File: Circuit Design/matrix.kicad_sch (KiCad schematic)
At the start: 198 parts

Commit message: all the routing is done
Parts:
- gave numbers to parts that had none: 198

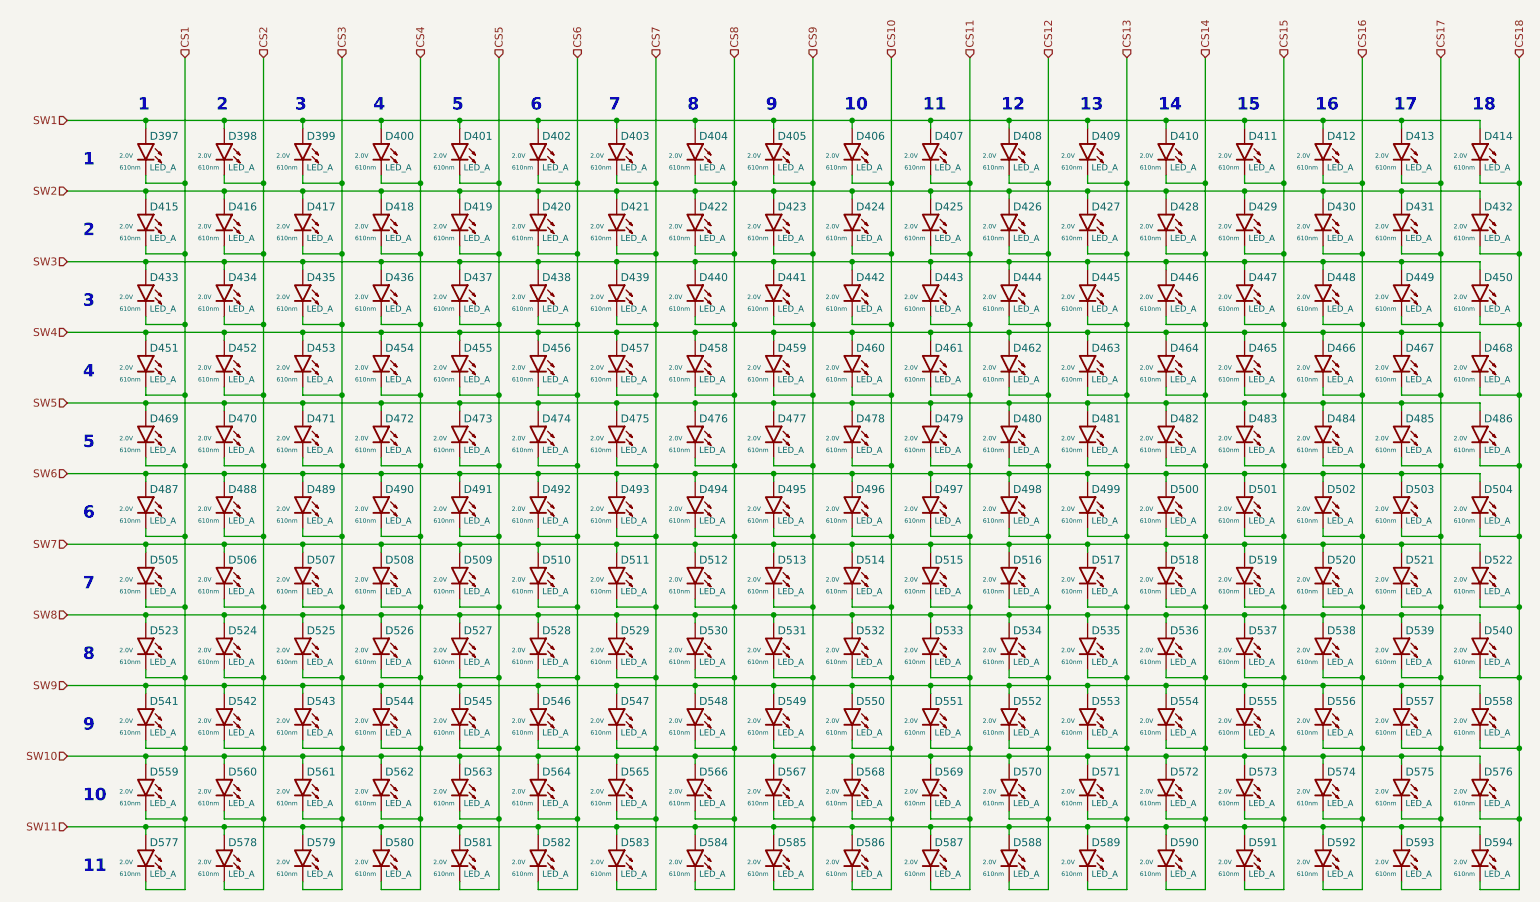
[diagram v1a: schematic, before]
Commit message: added IS31FL3731 and, edited its page
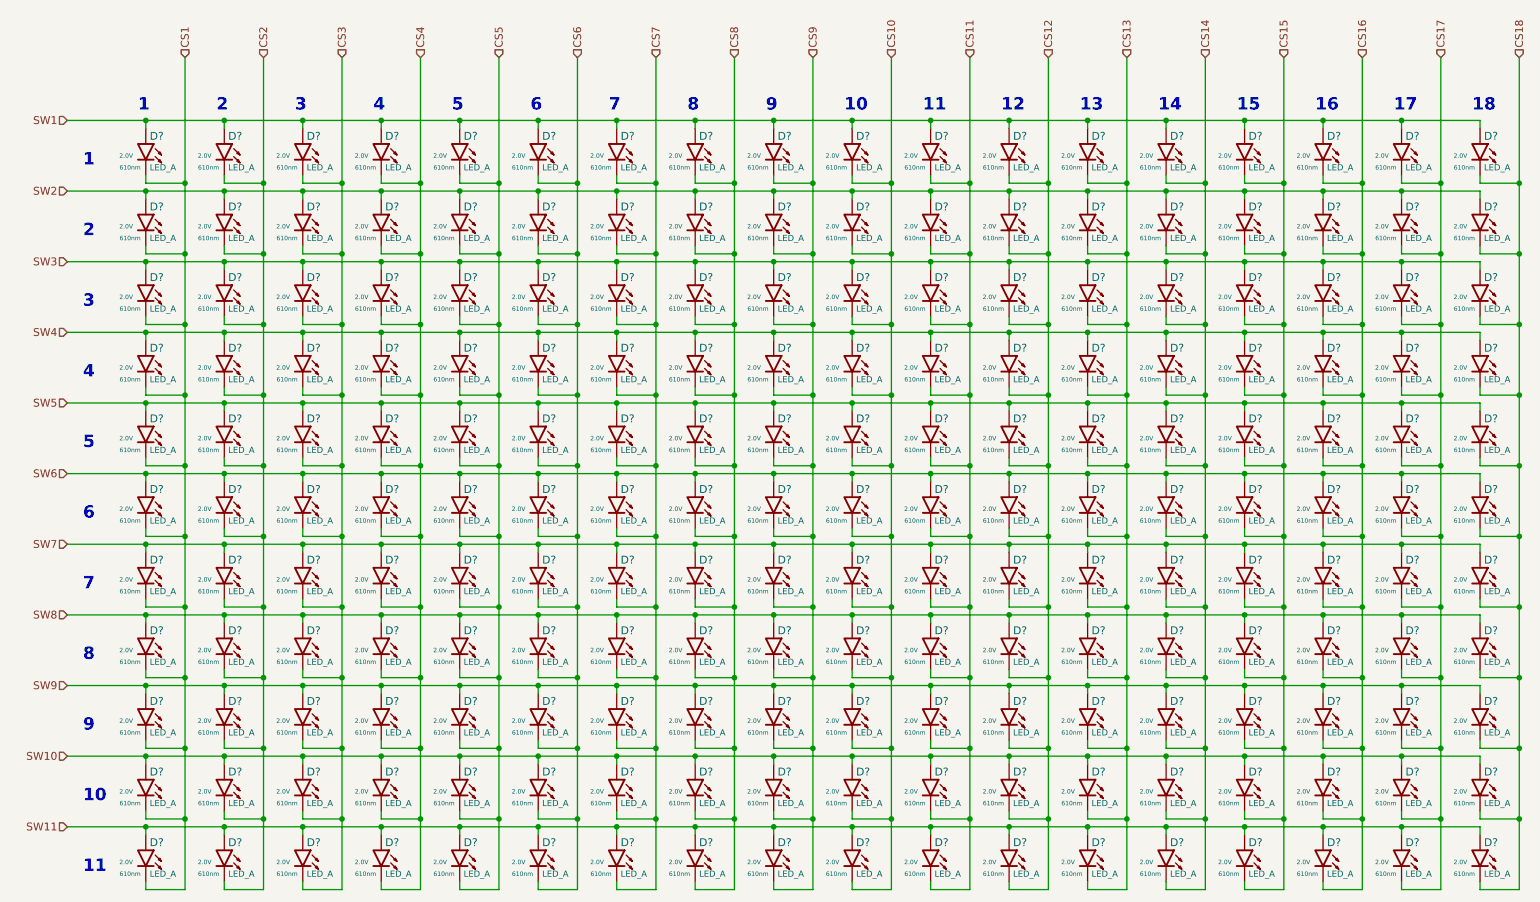
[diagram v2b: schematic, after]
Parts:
- renumbered D539 to D?, D530 to D?, D552 to D?, D586 to D?, D589 to D?, D459 to D?, D480 to D?, D506 to D?, D400 to D?, D527 to D?, D505 to D?, D487 to D?, D416 to D?, D572 to D?, D451 to D?, D435 to D?, D588 to D?, D469 to D?, D424 to D?, D534 to D?, D402 to D?, D520 to D?, D476 to D?, D526 to D?, D445 to D?, D502 to D?, D432 to D?, D462 to D?, D559 to D?, D446 to D?, D518 to D?, D512 to D?, D556 to D?, D563 to D?, D494 to D?, D524 to D?, D574 to D?, D428 to D?, D415 to D?, D580 to D?, D496 to D?, D399 to D?, D533 to D?, D444 to D?, D554 to D?, D472 to D?, D452 to D?, D427 to D?, D422 to D?, D564 to D?, D509 to D?, D522 to D?, D513 to D?, D417 to D?, D570 to D?, D503 to D?, D434 to D?, D409 to D?, D541 to D?, D557 to D?, D575 to D?, D508 to D?, D540 to D?, D404 to D?, D438 to D?, D493 to D?, D516 to D?, D519 to D?, D547 to D?, D555 to D?, D560 to D?, D529 to D?, D571 to D?, D486 to D?, D573 to D?, D455 to D?, D441 to D?, D591 to D?, D450 to D?, D420 to D?, D507 to D?, D490 to D?, D577 to D?, D514 to D?, D474 to D?, D465 to D?, D473 to D?, D544 to D?, D398 to D?, D443 to D?, D498 to D?, D517 to D?, D475 to D?, D423 to D?, D463 to D?, D483 to D?, D548 to D?, D397 to D?, D553 to D?, D403 to D?, D419 to D?, D590 to D?, D406 to D?, D414 to D?, D471 to D?, D479 to D?, D448 to D?, D511 to D?, D567 to D?, D426 to D?, D458 to D?, D562 to D?, D583 to D?, D464 to D?, D543 to D?, D457 to D?, D515 to D?, D531 to D?, D523 to D?, D500 to D?, D430 to D?, D453 to D?, D470 to D?, D576 to D?, D442 to D?, D407 to D?, D456 to D?, D538 to D?, D592 to D?, D551 to D?, D581 to D?, D521 to D?, D495 to D?, D549 to D?, D578 to D?, D466 to D?, D405 to D?, D594 to D?, D532 to D?, D566 to D?, D436 to D?, D558 to D?, D546 to D?, D439 to D?, D449 to D?, D525 to D?, D565 to D?, D413 to D?, D593 to D?, D569 to D?, D408 to D?, D440 to D?, D429 to D?, D510 to D?, D460 to D?, D501 to D?, D489 to D?, D431 to D?, D482 to D?, D550 to D?, D584 to D?, D537 to D?, D433 to D?, D484 to D?, D579 to D?, D536 to D?, D454 to D?, D545 to D?, D561 to D?, D478 to D?, D447 to D?, D461 to D?, D542 to D?, D410 to D?, D477 to D?, D491 to D?, D437 to D?, D528 to D?, D492 to D?, D421 to D?, D411 to D?, D485 to D?, D585 to D?, D488 to D?, D481 to D?, D412 to D?, D467 to D?, D425 to D?, D582 to D?, D499 to D?, D468 to D?, D535 to D?, D418 to D?, D568 to D?, D504 to D?, D497 to D?, D401 to D?, D587 to D?

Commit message: last commit before 0805 migration
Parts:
- removed D? (x198): LED_A, CoF_Diode:LED-0603, symbol CoE_Diode:LED_A
- added D1011, D1012, D1013, D1014, D1015, D1016, D1017, D1018, D1019, D1020, D1021, D1022, D1023, D1024, D1025, D1026, D1027, D1028, D1029, D1030, D1031, D1032, D1033, D1034, D1035, D1036, D1037, D1038, D1039, D1040, D1041, D1042, D1043, D1044, D1045, D1046, D1047, D1048, D1049, D1050, D1051, D1052, D1053, D1054, D1055, D1056, D1057, D1058, D1059, D1060, D1061, D1062, D1063, D1064, D1065, D1066, D1067, D1068, D1069, D1070, D1071, D1072, D1073, D1074, D1075, D1076, D1077, D1078, D1079, D1080, D1081, D1082, D1083, D1084, D1085, D1086, D1087, D1088, D1089, D1090, D1091, D1092, D1093, D1094, D1095, D1096, D1097, D1098, D1099, D1100, D1101, D1102, D1103, D1104, D1105, D1106, D1107, D1108, D1109, D1110, D1111, D1112, D1113, D1114, D1115, D1116, D1117, D1118, D1119, D1120, D1121, D1122, D1123, D1124, D1125, D1126, D1127, D1128, D1129, D1130, D1131, D1132, D1133, D1134, D1135, D1136, D1137, D1138, D1139, D1140, D1141, D1142, D1143, D1144, D1145, D1146, D1147, D1148, D1149, D1150, D1151, D1152, D1153, D1154: LED_O, CoF_Diode:LED-0402, symbol CoE_Diode:LED_O
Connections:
- new net CA1: D1011.1 (K), D1012.1 (K), D1013.1 (K), D1014.1 (K), D1015.1 (K), D1016.1 (K), D1017.1 (K), D1018.1 (K), D1027.2 (A), D1043.2 (A), D1059.2 (A), D1075.2 (A), D1091.2 (A), D1107.2 (A), D1123.2 (A), D1139.2 (A)
- new net CA2: D1011.2 (A), D1027.1 (K), D1028.1 (K), D1029.1 (K), D1030.1 (K), D1031.1 (K), D1032.1 (K), D1033.1 (K), D1034.1 (K), D1044.2 (A), D1060.2 (A), D1076.2 (A), D1092.2 (A), D1108.2 (A), D1124.2 (A), D1140.2 (A)
- new net CA3: D1012.2 (A), D1028.2 (A), D1043.1 (K), D1044.1 (K), D1045.1 (K), D1046.1 (K), D1047.1 (K), D1048.1 (K), D1049.1 (K), D1050.1 (K), D1061.2 (A), D1077.2 (A), D1093.2 (A), D1109.2 (A), D1125.2 (A), D1141.2 (A)
- new net CA4: D1013.2 (A), D1029.2 (A), D1045.2 (A), D1059.1 (K), D1060.1 (K), D1061.1 (K), D1062.1 (K), D1063.1 (K), D1064.1 (K), D1065.1 (K), D1066.1 (K), D1078.2 (A), D1094.2 (A), D1110.2 (A), D1126.2 (A), D1142.2 (A)
- new net CA5: D1014.2 (A), D1030.2 (A), D1046.2 (A), D1062.2 (A), D1075.1 (K), D1076.1 (K), D1077.1 (K), D1078.1 (K), D1079.1 (K), D1080.1 (K), D1081.1 (K), D1082.1 (K), D1095.2 (A), D1111.2 (A), D1127.2 (A), D1143.2 (A)
- new net CA6: D1015.2 (A), D1031.2 (A), D1047.2 (A), D1063.2 (A), D1079.2 (A), D1091.1 (K), D1092.1 (K), D1093.1 (K), D1094.1 (K), D1095.1 (K), D1096.1 (K), D1097.1 (K), D1098.1 (K), D1112.2 (A), D1128.2 (A), D1144.2 (A)
- new net CA7: D1016.2 (A), D1032.2 (A), D1048.2 (A), D1064.2 (A), D1080.2 (A), D1096.2 (A), D1107.1 (K), D1108.1 (K), D1109.1 (K), D1110.1 (K), D1111.1 (K), D1112.1 (K), D1113.1 (K), D1114.1 (K), D1129.2 (A), D1145.2 (A)
- new net CA8: D1017.2 (A), D1033.2 (A), D1049.2 (A), D1065.2 (A), D1081.2 (A), D1097.2 (A), D1113.2 (A), D1123.1 (K), D1124.1 (K), D1125.1 (K), D1126.1 (K), D1127.1 (K), D1128.1 (K), D1129.1 (K), D1130.1 (K), D1146.2 (A)
- new net CA9: D1018.2 (A), D1034.2 (A), D1050.2 (A), D1066.2 (A), D1082.2 (A), D1098.2 (A), D1114.2 (A), D1130.2 (A), D1139.1 (K), D1140.1 (K), D1141.1 (K), D1142.1 (K), D1143.1 (K), D1144.1 (K), D1145.1 (K), D1146.1 (K)
- new net CB1: D1019.1 (K), D1020.1 (K), D1021.1 (K), D1022.1 (K), D1023.1 (K), D1024.1 (K), D1025.1 (K), D1026.1 (K), D1035.2 (A), D1051.2 (A), D1067.2 (A), D1083.2 (A), D1099.2 (A), D1115.2 (A), D1131.2 (A), D1147.2 (A)
- new net CB2: D1019.2 (A), D1035.1 (K), D1036.1 (K), D1037.1 (K), D1038.1 (K), D1039.1 (K), D1040.1 (K), D1041.1 (K), D1042.1 (K), D1052.2 (A), D1068.2 (A), D1084.2 (A), D1100.2 (A), D1116.2 (A), D1132.2 (A), D1148.2 (A)
- new net CB3: D1020.2 (A), D1036.2 (A), D1051.1 (K), D1052.1 (K), D1053.1 (K), D1054.1 (K), D1055.1 (K), D1056.1 (K), D1057.1 (K), D1058.1 (K), D1069.2 (A), D1085.2 (A), D1101.2 (A), D1117.2 (A), D1133.2 (A), D1149.2 (A)
- new net CB4: D1021.2 (A), D1037.2 (A), D1053.2 (A), D1067.1 (K), D1068.1 (K), D1069.1 (K), D1070.1 (K), D1071.1 (K), D1072.1 (K), D1073.1 (K), D1074.1 (K), D1086.2 (A), D1102.2 (A), D1118.2 (A), D1134.2 (A), D1150.2 (A)
- new net CB5: D1022.2 (A), D1038.2 (A), D1054.2 (A), D1070.2 (A), D1083.1 (K), D1084.1 (K), D1085.1 (K), D1086.1 (K), D1087.1 (K), D1088.1 (K), D1089.1 (K), D1090.1 (K), D1103.2 (A), D1119.2 (A), D1135.2 (A), D1151.2 (A)
- new net CB6: D1023.2 (A), D1039.2 (A), D1055.2 (A), D1071.2 (A), D1087.2 (A), D1099.1 (K), D1100.1 (K), D1101.1 (K), D1102.1 (K), D1103.1 (K), D1104.1 (K), D1105.1 (K), D1106.1 (K), D1120.2 (A), D1136.2 (A), D1152.2 (A)
- new net CB7: D1024.2 (A), D1040.2 (A), D1056.2 (A), D1072.2 (A), D1088.2 (A), D1104.2 (A), D1115.1 (K), D1116.1 (K), D1117.1 (K), D1118.1 (K), D1119.1 (K), D1120.1 (K), D1121.1 (K), D1122.1 (K), D1137.2 (A), D1153.2 (A)
- new net CB8: D1025.2 (A), D1041.2 (A), D1057.2 (A), D1073.2 (A), D1089.2 (A), D1105.2 (A), D1121.2 (A), D1131.1 (K), D1132.1 (K), D1133.1 (K), D1134.1 (K), D1135.1 (K), D1136.1 (K), D1137.1 (K), D1138.1 (K), D1154.2 (A)
- new net CB9: D1026.2 (A), D1042.2 (A), D1058.2 (A), D1074.2 (A), D1090.2 (A), D1106.2 (A), D1122.2 (A), D1138.2 (A), D1147.1 (K), D1148.1 (K), D1149.1 (K), D1150.1 (K), D1151.1 (K), D1152.1 (K), D1153.1 (K), D1154.1 (K)
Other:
- note removed: "10"
- note removed: "11"
- note removed: "12"
- note removed: "13"
- note removed: "14"
- note removed: "15"
- note removed: "16"
- note removed: "17"
- note removed: "18"
